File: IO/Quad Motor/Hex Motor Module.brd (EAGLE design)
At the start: 25.4 x 25.4 mm, 3 parts

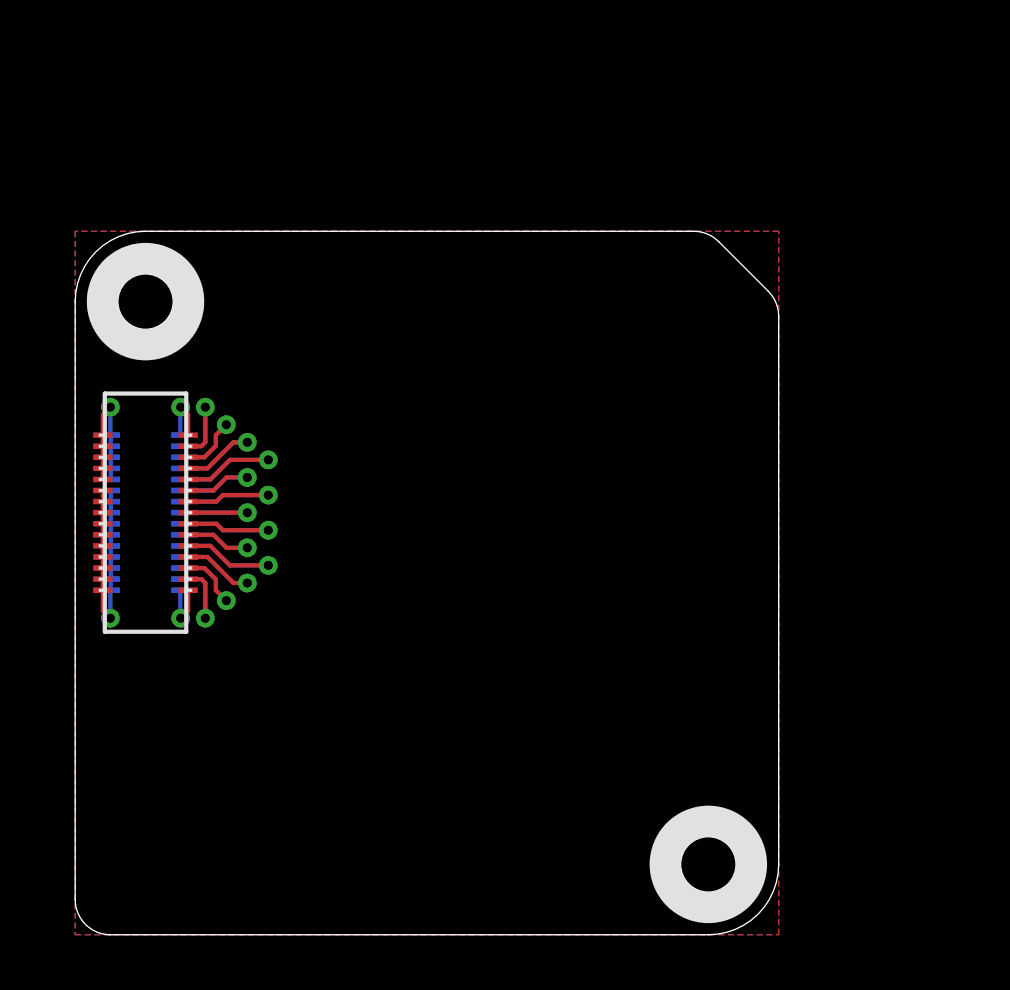
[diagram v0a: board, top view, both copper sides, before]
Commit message: Renamed file Hex Motor Module. Completed Schematic. Board layout and silkscreen needed.
Signed-off-by: Cruz Monrreal II <Cruz.Monrreal@gmail.com>
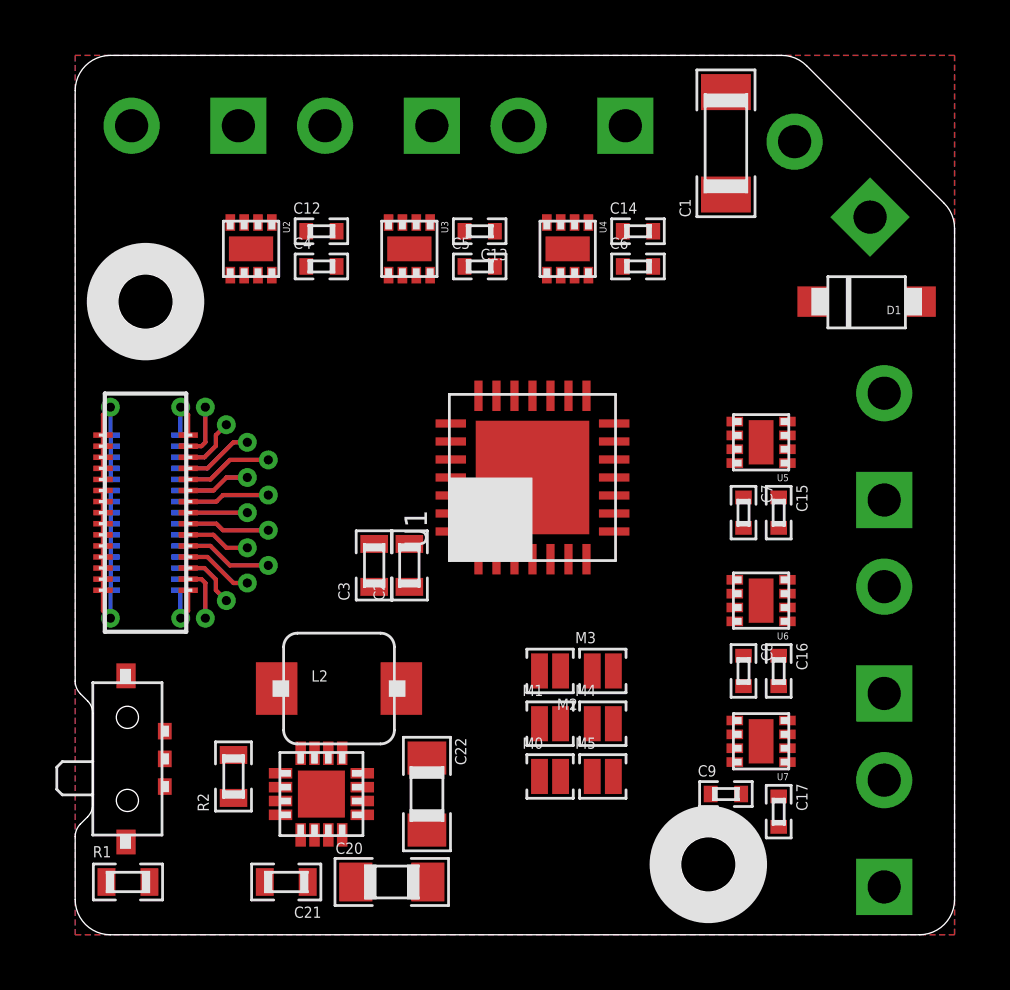
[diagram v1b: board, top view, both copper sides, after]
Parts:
- added C1: 10uF, .standardparts:1206
- added C12, C13, C14, C15, C16, C17, C4, C5, C6, C7, C8, C9: .1uF, .standardparts:0402
- added C2: .1uF, .standardparts:0603
- added C20, C22: 10uF, .standardparts:0805
- added C21: 3.3nF, .standardparts:0603
- added C3: 1uF, .standardparts:0603
- added D1: (no value), nxp:SOD123W
- added JP1, JP2, JP3, JP4, JP5, JP6, JP7: (no value), SparkFun:SCREWTERMINAL-3.5MM-2_LOCK
- added L2: 2.2uH, bourns:SRP4020
- added M0, M1, M2, M3, M4, M5: (no value), .solderjumper:2.LRG.PASTE
- added R1, R2: 100k, .standardparts:0603
- added U$44: SSAJ110100, alps:SSAJ110100
- added U1: PCA9685, nxp:HVQFN28
- added U10: TPS62142, .packages(ti):RGT
- added U2, U3, U4, U5, U6, U7: DRV8837, .packages(ti):DSG
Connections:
- new net !OE: R1.2, U$44.C, U1.23
- new net M0.A: U1.21, U2.6
- new net M0.B: U1.22, U2.5
- new net M0.EN: M0.2, U2.7
- new net M1.A: U1.19, U3.6
- new net M1.B: U1.20, U3.5
- new net M1.EN: M1.2, U3.7
- new net M2.A: U1.17, U4.6
- new net M2.B: U1.18, U4.5
- new net M2.EN: M2.2, U4.7
- new net M3.A: U1.15, U5.6
- new net M3.B: U1.16, U5.5
- new net M3.EN: M3.2, U5.7
- new net M4.A: U1.12, U6.6
- new net M4.B: U1.13, U6.5
- new net M4.EN: M4.2, U6.7
- new net M5.A: U1.10, U7.6
- new net M5.B: U1.11, U7.5
- new net M5.EN: M5.2, U7.7
- new net N$16: JP1.1, U2.2
- new net N$17: JP1.2, U2.3
- new net N$18: JP4.1, U5.2
- new net N$19: JP4.2, U5.3
- new net N$20: JP5.1, U6.2
- new net N$21: JP5.2, U6.3
- new net N$22: JP6.1, U7.2
- new net N$23: JP6.2, U7.3
- new net N$24: JP3.1, U4.2
- new net N$25: JP3.2, U4.3
- new net N$26: JP2.1, U3.2
- new net N$27: JP2.2, U3.3
- new net N$32: D1.P$1, JP7.1
- new net N$33: C21.1, U10.9
- new net SCL: U$8.SCL, U$8.SCL@1, U$8.SCL@VIA, U1.26
- new net SDA: U$8.SDA, U$8.SDA@1, U$8.SDA@VIA, U1.27
- new net VIN: C1.1, C12.1, C13.1, C14.1, C15.1, C16.1, C17.1, C20.1, D1.P$2, U10.10, U10.11, U10.12, U10.13, U2.1, U3.1, U4.1, U5.1, U6.1, U7.1
- net 3.3V: now also C2.1, C22.1, C3.1, C4.1, C5.1, C6.1, C7.1, C8.1, C9.1, L2.2, M0.1, M1.1, M2.1, M3.1, M4.1, M5.1, R1.1, R2.1, U1.24, U1.28, U10.14, U2.8, U3.8, U4.8, U5.8, U6.8, U7.8
- net GND: now also C1.2, C12.2, C13.2, C14.2, C15.2, C16.2, C17.2, C2.2, C20.2, C21.2, C22.2, C3.2, C4.2, C5.2, C6.2, C7.2, C8.2, C9.2, JP7.2, U$44.1, U1.1, U1.14, U1.2, U1.25, U1.3, U1.4, U1.5, U1.PAD, U10.15, U10.16, U10.5, U10.6, U10.7, U10.8, U10.PAD, U2.4, U2.PAD, U3.4, U3.PAD, U4.4, U4.PAD, U5.4, U5.PAD, U6.4, U6.PAD, U7.4, U7.PAD
- net N$3: now also L2.1, U10.1, U10.2, U10.3; no longer U$8.SDA, U$8.SDA@1, U$8.SDA@VIA
- net N$4: now also R2.2, U10.4; no longer U$8.SCL, U$8.SCL@1, U$8.SCL@VIA
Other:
- board size 25.4 x 25.4 mm -> 31.8 x 31.8 mm
